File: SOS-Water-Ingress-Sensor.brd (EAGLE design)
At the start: 24.3 x 13 mm, 12 parts

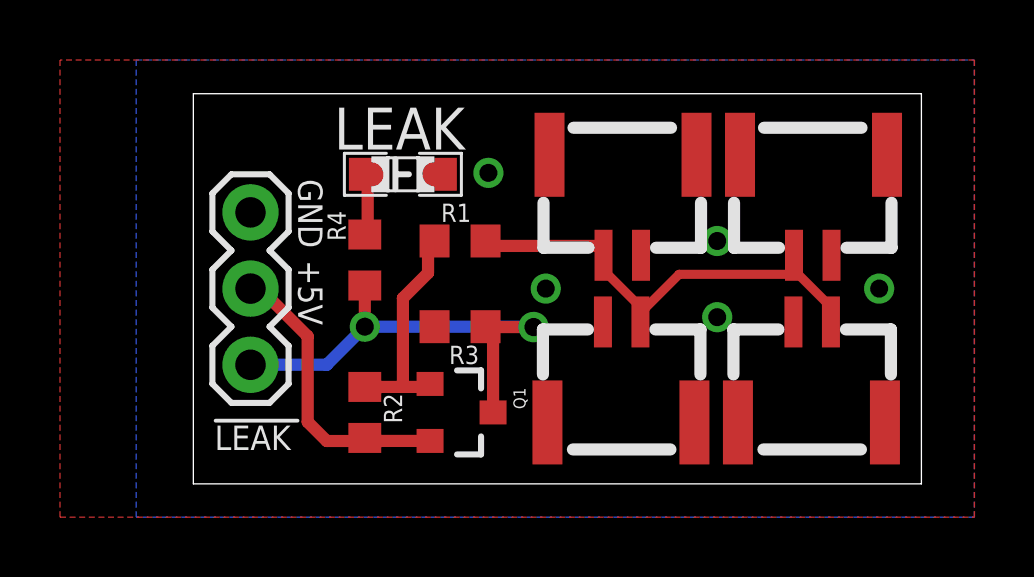
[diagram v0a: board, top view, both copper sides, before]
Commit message: Change component values and layout.
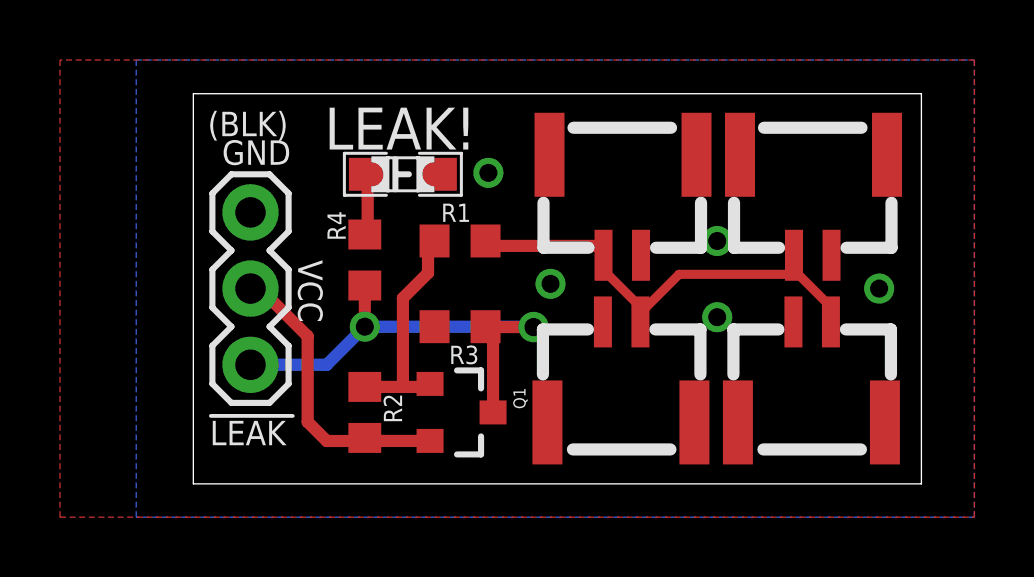
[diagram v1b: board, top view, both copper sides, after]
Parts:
- R1: value 10K -> 1K
- R2: value 12K -> 27K
- R3: value 2.2K -> 1K
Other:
- board text added: "(BLK)"
- board text added: "LEAK!"
- board text added: "VCC"
- board text added: "rev2"
- board text removed: "+5V"
- board text removed: "rev1"
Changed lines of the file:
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@@
 <wire x1="24.90375" y1="12.84625" x2="0.635" y2="12.84625" width="0" layer="20"/>
 <wire x1="0.635" y1="12.84625" x2="0.635" y2="-0.15875" width="0" layer="20"/>
-<text x="5.3260625" y="10.9855" size="1.397" layer="25" ratio="12">LEAK</text>
-<text x="24.145875" y="7.699375" size="0.635" layer="26" ratio="12" rot="MR0">rev1</text>
+<text x="5.0085625" y="10.9855" size="1.397" layer="25" ratio="12">LEAK!</text>
+<text x="24.145875" y="8.651875" size="0.635" layer="26" ratio="12" rot="MR0">rev2</text>
 <text x="5.9769375" y="0.6985" size="0.635" layer="26" ratio="12" rot="MR0">A.S. 8/16</text>
-<text x="24.13" y="8.89" size="1.27" layer="26" ratio="12" rot="MR0">SOS Leak Sensor
+<text x="24.13" y="9.8425" size="0.8128" layer="26" ratio="12" rot="MR0">SOS Leak Sensor
 Probe Host Board</text>
-<text x="4.1275" y="10.00125" size="0.8128" layer="25" ratio="12" rot="SR270">GND</text>
-<text x="4.1275" y="7.3025" size="0.8128" layer="25" ratio="12" rot="SR270">+5V</text>
-<text x="1.3425" y="0.970234375" size="0.8128" layer="21" ratio="12">LEAK</text>
-<wire x1="1.377953125" y1="1.947603125" x2="4.10818125" y2="1.947603125" width="0.127" layer="21"/>
+<text x="1.5875" y="10.4775" size="0.8128" layer="25" ratio="12" rot="SR0">GND</text>
+<text x="4.1275" y="7.3025" size="0.8128" layer="25" ratio="12" rot="SR270">VCC</text>
+<text x="1.18375" y="1.128984375" size="0.8128" layer="21" ratio="12">LEAK</text>
+<wire x1="1.219203125" y1="2.106353125" x2="3.94943125" y2="2.106353125" width="0.127" layer="21"/>
 <text x="6.19125" y="8.5725" size="0.8128" layer="26" ratio="12" rot="SMR0">GND</text>
-<text x="6.19125" y="5.87375" size="0.8128" layer="26" ratio="12" rot="SMR0">+5V</text>
+<text x="6.19125" y="5.87375" size="0.8128" layer="26" ratio="12" rot="SMR0">VCC</text>
 <text x="6.969125" y="3.33375" size="0.8128" layer="22" ratio="12" rot="MR0">LEAK</text>
 <wire x1="4.1671875" y1="4.3259375" x2="6.9770625" y2="4.3259375" width="0.127" layer="22"/>
 <text x="21.3915625" y="1.6748125" size="1.016" layer="22" ratio="12" rot="MR0">BlueRobotics</text>
+<text x="1.11125" y="11.43" size="0.8128" layer="25" ratio="12" rot="SR0">(BLK)</text>
 </plain>
 <attributes>
@@
 <elements>
 <element name="U$7" library="BR-Eagle-Library" package="BR-LOGO-SMALL" value="LOGOBR-LOGO-S" x="24.28875" y="0.9525" rot="MR0"/>
-<element name="R2" library="resistor" package="R0603" value="12K" x="6.35" y="2.2225" rot="R270"/>
-<element name="R1" library="resistor" package="R0603" value="10K" x="9.525" y="7.9375"/>
+<element name="R2" library="resistor" package="R0603" value="27K" x="6.35" y="2.2225" rot="R270"/>
+<element name="R1" library="resistor" package="R0603" value="1K" x="9.525" y="7.9375"/>
 <element name="U$1" library="BlueRobotics-JST-GH" package="JST-GH-TOP-2" value="JSH-GH-2VERT" x="14.2875" y="5.23875"/>
 <element name="Q1" library="SparkFun-DiscreteSemi" package="SOT23-3" value="" x="9.525" y="2.2225" rot="R270"/>
-<element name="R3" library="resistor" package="R0603" value="2.2K" x="9.525" y="5.08" rot="R180"/>
+<element name="R3" library="resistor" package="R0603" value="1K" x="9.525" y="5.08" rot="R180"/>
 <element name="U$2" library="BlueRobotics-JST-GH" package="JST-GH-TOP-2" value="JSH-GH-2VERT" x="20.6375" y="5.23875"/>
 <element name="U$3" library="BlueRobotics-JST-GH" package="JST-GH-TOP-2" value="JSH-GH-2VERT" x="15.5575" y="7.46125" rot="R180"/>
@@
 </polygon>
 <via x="10.4695625" y="10.207625" extent="1-16" drill="0.6"/>
-<via x="12.3825" y="6.35" extent="1-16" drill="0.6"/>
+<via x="12.54125" y="6.50875" extent="1-16" drill="0.6"/>
 <via x="18.0975" y="7.9375" extent="1-16" drill="0.6"/>
 <via x="18.0975" y="5.3975" extent="1-16" drill="0.6"/>
